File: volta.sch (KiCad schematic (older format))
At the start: 7 parts, among them J1 , J2 , T1 5:1 - 5A

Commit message: Trabajo
 Cambios para hacer commit:
	modificado:    volta-cache.lib
	modificado:    volta.kicad_pcb
	modificado:    volta.pro
	modificado:    volta.sch
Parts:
- removed J1, J2: (no value), Pin_Headers:Pin_Header_Straight_1x01_Pitch2.54mm, symbol Conn_01x01_Female
- removed T1: 5:1 - 5A, TerminalBlock:TerminalBlock_bornier-5_P5.08mm, symbol Transformer_1P_SS
- added C10, C6: 1uF, Capacitors_THT:CP_Radial_D5.0mm_P2.00mm, symbol EXI_Condensador_Polarizado
- added C11: 10uF, Capacitors_THT:CP_Radial_D5.0mm_P2.00mm, symbol EXI_Condensador_Polarizado
- added C3, C7: 0.33uF, Capacitors_THT:CP_Radial_D5.0mm_P2.00mm, symbol EXI_Condensador
- added C4, C8, C9: 0.1uF, Capacitors_THT:C_Disc_D5.0mm_W2.5mm_P2.50mm, symbol EXI_Condensador
- added C5: 22uF / 25V, Capacitors_THT:CP_Radial_D5.0mm_P2.00mm, symbol EXI_Condensador_Polarizado
- added D2, D3, D4, D5, D6: 1N4007, Diodes_THT:D_DO-41_SOD81_P10.16mm_Horizontal, symbol EXI_1N4007
- added J1: AC-vivo, EXI_Conectores:EXI_Pad_6x7mm_x1, symbol Conn_01x01
- added J10: +Vv, EXI_Conectores:EXI_Pad_6x7mm_x1, symbol Conn_01x01
- added J11: +5V, EXI_Conectores:EXI_Pad_6x7mm_x1, symbol Conn_01x01
- added J2: Trans-Vivo, EXI_Conectores:EXI_Pad_6x7mm_x1, symbol Conn_01x01
- added J3: Deriv, EXI_Conectores:EXI_Pad_6x7mm_x1, symbol Conn_01x01
- added J4: Trans-V24, EXI_Conectores:EXI_Pad_6x7mm_x1, symbol Conn_01x01
- added J5: Trans-N24, EXI_Conectores:EXI_Pad_6x7mm_x1, symbol Conn_01x01
- added J6: GND, EXI_Conectores:EXI_Pad_6x7mm_x1, symbol Conn_01x01
- added J7: V-, EXI_Conectores:EXI_Pad_6x7mm_x1, symbol Conn_01x01
- added J8: +12, EXI_Conectores:EXI_Pad_6x7mm_x1, symbol Conn_01x01
- added J9: -12, EXI_Conectores:EXI_Pad_6x7mm_x1, symbol Conn_01x01
- added MK1, MK2, MK3, MK4: Mounting_Hole, EXI_Montaje:Tuerca_9mm, symbol Mounting_Hole
- added POT1: 5k, TerminalBlock:TerminalBlock_bornier-3_P5.08mm, symbol EXI_Potenciómetro
- added POT2: 1k, TerminalBlock:TerminalBlock_bornier-3_P5.08mm, symbol EXI_Potenciómetro
- added R1: 120, Resistors_THT:R_Axial_DIN0309_L9.0mm_D3.2mm_P12.70mm_Horizontal, symbol EXI_Resistor
- added U1: L7812, EXI_Transistores:TO-220-3_Horizontal_Heatsink_10x15x21mm, symbol L7812
- added U2: L7912, EXI_Transistores:TO-220-3_Horizontal_Heatsink_10x15x21mm, symbol L7912
- added U3: L7805, EXI_Transistores:TO-220-3_Horizontal_Heatsink_10x15x21mm, symbol L7805
- added U4: LM338T, EXI_Transistores:TO-220-3_Horizontal_Heatsink_10x15x21mm, symbol LM338T
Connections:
- net labels added: +12, +12V, +5V, +Vv, -12, -12V, 120vAC / 60 hZ, 5:1 - 5A, Común, GNDPWR, Interruptor / Selector, LINE, NEUT, V+, V-, comun
- net labels removed: 120V / 60Hz
- wire segments 21 -> 93
- no-connect marks 0 -> 2
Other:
- moved on the sheet: C1, C2, D1, F1

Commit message: Cambios menores
 Cambios para hacer commit:
	agregado el modelo 3D del pin hecho en Wings3D al pcb
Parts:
- J1: footprint EXI_Conectores:EXI_Pad_6x7mm_x1 -> EXI_Conectores:terminal_faston_0.25

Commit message: Actualización
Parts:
- removed POT1: 5k, TerminalBlock:TerminalBlock_bornier-3_P5.08mm, symbol EXI_Potenciómetro
- removed POT2: 1k, TerminalBlock:TerminalBlock_bornier-3_P5.08mm, symbol EXI_Potenciómetro
- added J6: Pot_adj, EXI_Conectores:terminal_faston_0.25, symbol Conn_01x01
- added J7: Pot_gnd, EXI_Conectores:terminal_faston_0.25, symbol Conn_01x01
- added LED1: Activo, Pin_Headers:Pin_Header_Straight_1x02_Pitch2.54mm, symbol EXI_LED
- added R2: 470, Resistors_THT:R_Axial_DIN0309_L9.0mm_D3.2mm_P12.70mm_Horizontal, symbol EXI_Resistor
- added V1: EXI_Ventilador, symbol EXI_Ventilador
- J10: renamed from J8; footprint EXI_Conectores:EXI_Pad_6x7mm_x1 -> EXI_Conectores:terminal_faston_0.25
- J11: renamed from J9; footprint EXI_Conectores:EXI_Pad_6x7mm_x1 -> EXI_Conectores:terminal_faston_0.25
- J12: renamed from J10; footprint EXI_Conectores:EXI_Pad_6x7mm_x1 -> EXI_Conectores:terminal_faston_0.25
- J13: renamed from J11; footprint EXI_Conectores:EXI_Pad_6x7mm_x1 -> EXI_Conectores:terminal_faston_0.25
- J2: footprint EXI_Conectores:EXI_Pad_6x7mm_x1 -> EXI_Conectores:terminal_faston_0.25
- J3: renamed from J4; footprint EXI_Conectores:EXI_Pad_6x7mm_x1 -> EXI_Conectores:terminal_faston_0.25
- J4: renamed from J5; footprint EXI_Conectores:EXI_Pad_6x7mm_x1 -> EXI_Conectores:terminal_faston_0.25
- J5: renamed from J3; footprint EXI_Conectores:EXI_Pad_6x7mm_x1 -> EXI_Conectores:terminal_faston_0.25
- J8: renamed from J6; footprint EXI_Conectores:EXI_Pad_6x7mm_x1 -> EXI_Conectores:terminal_faston_0.25
- J9: renamed from J7; footprint EXI_Conectores:EXI_Pad_6x7mm_x1 -> EXI_Conectores:terminal_faston_0.25
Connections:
- net +5V: now also R2.1, V1.1 (+)
- net GND: now also V1.2 (-)
- net comun: now also J7.1 (Pin_1), LED1.2 (C)
- net sw: now reaches F1.1, J1.1 (Pin_1)
- net trans: now reaches F1.2, J2.1 (Pin_1)
- net v24: now reaches D1.2 (ac), J3.1 (Pin_1)
- net n24: now reaches D1.3 (ac), J4.1 (Pin_1)
- net adj: now reaches C11.1, D6.1 (A), R1.2, U4.1 (Adj)
- net adj: now also J6.1 (Pin_1)
- new net: LED1.1 (A), R2.2
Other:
- moved on the sheet: F1, J1, J2, J3, J4, J5

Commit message: Actualización mayor
cambio de pin blade 3.6
cambio de capacitores 3.3uF
cambio de pines para potenciometros
cambio de huella para fusible
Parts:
- removed C1, C2: 2200uF / 50V, Capacitors_THT:CP_Radial_D16.0mm_P7.50mm, symbol EXI_Condensador_Polarizado
- removed C10, C6: 1uF, Capacitors_THT:CP_Radial_D5.0mm_P2.00mm, symbol EXI_Condensador_Polarizado
- removed C11: 10uF, Capacitors_THT:CP_Radial_D5.0mm_P2.00mm, symbol EXI_Condensador_Polarizado
- removed C3, C7: 0.33uF, Capacitors_THT:CP_Radial_D5.0mm_P2.00mm, symbol EXI_Condensador
- removed C4, C8, C9: 0.1uF, Capacitors_THT:C_Disc_D5.0mm_W2.5mm_P2.50mm, symbol EXI_Condensador
- removed C5: 22uF / 25V, Capacitors_THT:CP_Radial_D5.0mm_P2.00mm, symbol EXI_Condensador_Polarizado
- removed D2, D3, D4, D5, D6: 1N4007, Diodes_THT:D_DO-41_SOD81_P10.16mm_Horizontal, symbol EXI_1N4007
- removed F1: Fusible, Fuse_Holders_and_Fuses:Fuseholder5x20_horiz_open_inline_Type-I, symbol EXI_Fusible
- removed LED1: Activo, Pin_Headers:Pin_Header_Straight_1x02_Pitch2.54mm, symbol EXI_LED
- removed R1: 120, Resistors_THT:R_Axial_DIN0309_L9.0mm_D3.2mm_P12.70mm_Horizontal, symbol EXI_Resistor
- removed R2: 470, Resistors_THT:R_Axial_DIN0309_L9.0mm_D3.2mm_P12.70mm_Horizontal, symbol EXI_Resistor
- added C1, C2: 2200uF / 50V, Capacitors_THT:CP_Radial_D16.0mm_P7.50mm, symbol CP
- added C10, C6: 1uF, Capacitors_THT:CP_Radial_D5.0mm_P2.00mm, symbol CP
- added C11: 10uF, Capacitors_THT:CP_Radial_D5.0mm_P2.00mm, symbol CP
- added C3, C7: 0.33uF, Capacitors_THT:C_Disc_D9.0mm_W2.5mm_P5.00mm, symbol C
- added C4, C8, C9: 0.1uF, Capacitors_THT:C_Disc_D5.0mm_W2.5mm_P2.50mm, symbol C
- added C5: 22uF, Capacitors_THT:CP_Radial_D5.0mm_P2.00mm, symbol CP
- added D2, D3, D4, D5, D6: 1N4007, Diodes_THT:D_DO-41_SOD81_P7.62mm_Horizontal, symbol 1N4007
- added D7: Activo, Pin_Headers:Pin_Header_Straight_1x02_Pitch2.54mm, symbol LED
- added F1: Fusible, Fuse_Holders_and_Fuses:Fuseholder5x20_horiz_open_universal_Type-III, symbol Fuse
- added R1: 120, Resistors_THT:R_Axial_DIN0309_L9.0mm_D3.2mm_P12.70mm_Horizontal, symbol R
- added R2: 470, Resistors_THT:R_Axial_DIN0309_L9.0mm_D3.2mm_P12.70mm_Horizontal, symbol R
- J1, J10, J11, J12, J13, J2, J3, J4, J5, J8, J9: footprint EXI_Conectores:terminal_faston_0.25 -> EXI_Conectores:blade_vertical_6.3mm_P5.08mm
- J6, J7: footprint EXI_Conectores:terminal_faston_0.25 -> Pin_Headers:Pin_Header_Straight_1x01_Pitch2.54mm
- V1: footprint (none) -> Pin_Headers:Pin_Header_Straight_1x02_Pitch2.54mm
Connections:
- net +12: now also C4.1, D2.1 (K)
- net +5V: now also C8.1, D4.1 (K), R2.1
- net +Vv: now also C10.1, D5.2 (A), D6.1 (K), R1.1
- net -12: now also C6.2, D3.2 (A)
- net GND: now also C1.2, C2.1, C3.2, C4.2, C5.1, C6.1, D2.2 (A), D3.1 (K); no longer V1.2 (-)
- net V-: now also C2.2; no longer U2.2 (VI)
- net adj: now also C11.1, D6.2 (A), R1.2
- net comun: no longer U3.2 (GND)
- net sw: now also F1.2
- net trans: now also F1.1
- net V+ renamed +VDC
- net +VDC: now also C1.1, C3.1, C7.1, C9.1, D5.1 (K)
- new net: D7.2 (A), R2.2
- new net -VDC: C5.2, U2.2 (VI)
- new net GNDREF: C10.2, C11.2, C7.2, C8.2, C9.2, D4.2 (A), D7.1 (K), U3.2 (GND), V1.2 (-)
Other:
- note added: "Extras"
- note added: "Reducción, Rectificación y Filtrado"
- note added: "Referencias"
- note added: "Regulación Variable"
- note added: "Regulación fija +5V"
- note added: "Regulación simétrica +/- 12V"
- note added: "Selector de salidas"
- note removed: "Alimentaciones"
- moved on the sheet: D1, J1, J10, J11, J12, J13, J2, J3, J4, J5, J6, J7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

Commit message: nuevo cajetin de udeg
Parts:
- removed D7: Activo, Pin_Headers:Pin_Header_Straight_1x02_Pitch2.54mm, symbol LED
- removed J6: Pot_adj, Pin_Headers:Pin_Header_Straight_1x01_Pitch2.54mm, symbol Conn_01x01
- removed J7: Pot_gnd, Pin_Headers:Pin_Header_Straight_1x01_Pitch2.54mm, symbol Conn_01x01
- removed V1: EXI_Ventilador, Pin_Headers:Pin_Header_Straight_1x02_Pitch2.54mm, symbol EXI_Ventilador
- added J101: Perifericos, Pin_Headers:Pin_Header_Straight_1x04_Pitch2.54mm, symbol Conn_01x04
- C10: footprint Capacitors_THT:CP_Radial_D5.0mm_P2.00mm -> Capacitors_THT:CP_Radial_D5.0mm_P2.50mm
- C3, C4, C7, C8, C9: symbol C -> C-RESCUE-volta
- R1, R2: symbol R -> R-RESCUE-volta
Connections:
- net +5V: now also J101.4 (Pin_4)
- net GNDREF: now also J101.1 (Pin_1)
- net adj: now also J101.2 (Pin_2)
- net LED: now reaches R2.2
- net LED: now also J101.3 (Pin_3)

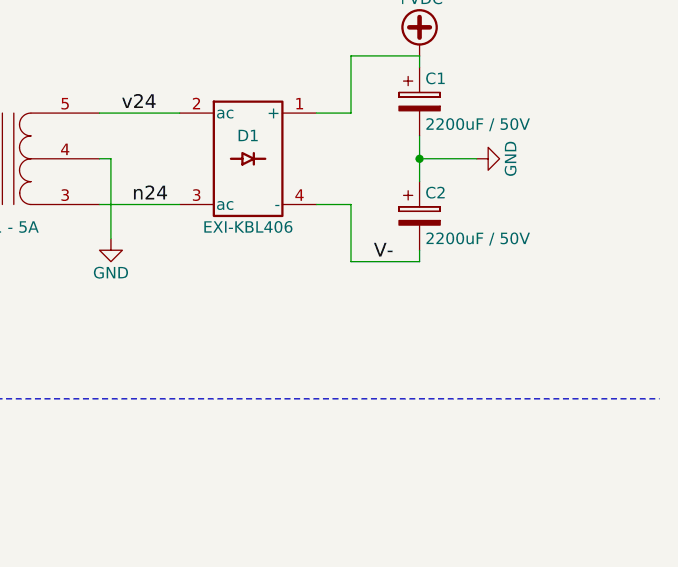
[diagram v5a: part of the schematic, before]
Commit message: avanzada en la PCB con plano de tierra
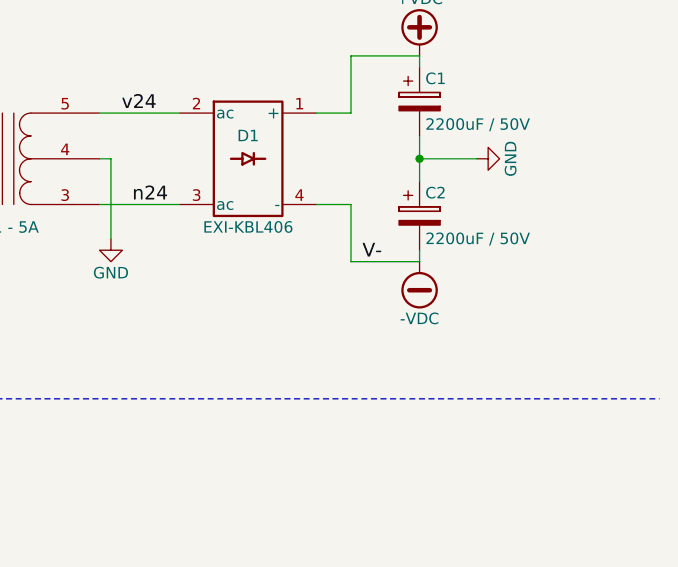
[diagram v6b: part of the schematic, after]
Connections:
- net V- is gone; now on net -VDC: C2.2, D1.4 (-), J9.1 (Pin_1)
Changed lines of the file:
@@
 LIBS:EXI_Transistores
 LIBS:EXI_Varios
-LIBS:Amplifier_Audio
-LIBS:Amplifier_Buffer
-LIBS:Amplifier_Current
-LIBS:Amplifier_Difference
-LIBS:Amplifier_Instrumentation
-LIBS:Amplifier_Operational
-LIBS:Amplifier_Video
-LIBS:Analog
-LIBS:Analog_ADC
-LIBS:Analog_DAC
-LIBS:Analog_Switch
-LIBS:Audio
-LIBS:Battery_Management
-LIBS:Comparator
-LIBS:Connector_Generic
-LIBS:Connector_Generic_Shielded
-LIBS:Connector_Specialized
-LIBS:Converter_ACDC
-LIBS:Converter_DCDC
-LIBS:CPLD_Altera
-LIBS:CPLD_Xilinx
-LIBS:CPU
-LIBS:CPU_NXP_6800
-LIBS:CPU_NXP_68000
-LIBS:CPU_PowerPC
-LIBS:Device
-LIBS:Diode
-LIBS:Diode_Bridge
-LIBS:Diode_Laser
-LIBS:Display_Character
-LIBS:Display_Graphic
-LIBS:Driver_Display
-LIBS:Driver_FET
-LIBS:Driver_LED
-LIBS:Driver_Motor
-LIBS:Driver_Relay
-LIBS:DSP_Freescale
-LIBS:DSP_Microchip_DSPIC33
-LIBS:DSP_Motorola
-LIBS:DSP_Texas
-LIBS:Filter
-LIBS:FPGA_Actel
-LIBS:FPGA_Xilinx
-LIBS:FPGA_Xilinx_Artix7
-LIBS:FPGA_Xilinx_Kintex7
-LIBS:FPGA_Xilinx_Spartan6
-LIBS:FPGA_Xilinx_Virtex5
-LIBS:FPGA_Xilinx_Virtex6
-LIBS:FPGA_Xilinx_Virtex7
-LIBS:GPU
-LIBS:Graphic
-LIBS:Interface
-LIBS:Interface_CAN_LIN
-LIBS:Interface_CurrentLoop
-LIBS:Interface_Ethernet
-LIBS:Interface_Expansion
-LIBS:Interface_HID
-LIBS:Interface_LineDriver
-LIBS:Interface_Optical
-LIBS:Interface_Telecom
-LIBS:Interface_UART
-LIBS:Interface_USB
-LIBS:Isolator
-LIBS:Isolator_Analog
-LIBS:Jumper
-LIBS:LED
-LIBS:Logic_74xgxx
-LIBS:Logic_74xx
-LIBS:Logic_CMOS_4000
-LIBS:Logic_CMOS_IEEE
-LIBS:Logic_LevelTranslator
-LIBS:Logic_Programmable
-LIBS:Logic_TTL_IEEE
-LIBS:MCU_AnalogDevices
-LIBS:MCU_Atmel_8051
-LIBS:MCU_Atmel_ATMEGA
-LIBS:MCU_Atmel_ATTINY
-LIBS:MCU_Atmel_AVR
-LIBS:MCU_Cypress
-LIBS:MCU_Infineon
-LIBS:MCU_Intel
-LIBS:MCU_Microchip_PIC10
-LIBS:MCU_Microchip_PIC12
-LIBS:MCU_Microchip_PIC16
-LIBS:MCU_Microchip_PIC18
-LIBS:MCU_Microchip_PIC24
-LIBS:MCU_Microchip_PIC32
-LIBS:MCU_Microchip_SAME
-LIBS:MCU_Microchip_SAML
-LIBS:MCU_Module
-LIBS:MCU_NXP_ColdFire
-LIBS:MCU_NXP_HC11
-LIBS:MCU_NXP_HC12
-LIBS:MCU_NXP_HCS12
-LIBS:MCU_NXP_Kinetis
-LIBS:MCU_NXP_LPC
-LIBS:MCU_NXP_MAC7100
-LIBS:MCU_NXP_MCore
-LIBS:MCU_NXP_S08
-LIBS:MCU_Parallax
-LIBS:MCU_SiFive
-LIBS:MCU_SiliconLabs
-LIBS:MCU_ST_STM8
-LIBS:MCU_ST_STM32
-LIBS:MCU_Texas
-LIBS:MCU_Texas_MSP430
-LIBS:Mechanical
-LIBS:Memory_Controller
-LIBS:Memory_EEPROM
-LIBS:Memory_EPROM
-LIBS:Memory_Flash
-LIBS:Memory_NVRAM
-LIBS:Memory_RAM
-LIBS:Memory_ROM
-LIBS:Memory_UniqueID
-LIBS:Motor
-LIBS:Oscillator
-LIBS:Potentiometer_Digital
 LIBS:power
 LIBS:Power_Management
-LIBS:Power_Protection
-LIBS:Power_Supervisor
 LIBS:pspice
-LIBS:Reference_Current
-LIBS:Reference_Voltage
-LIBS:Regulator_Controller
-LIBS:Regulator_Current
-LIBS:Regulator_Linear
-LIBS:Regulator_SwitchedCapacitor
-LIBS:Regulator_Switching
-LIBS:Relay
-LIBS:Relay_SolidState
-LIBS:RF
-LIBS:RF_AM_FM
-LIBS:RF_Bluetooth
-LIBS:RF_GPS
-LIBS:RF_Mixer
-LIBS:RF_Module
-LIBS:RF_RFID
-LIBS:RF_WiFi
-LIBS:RF_ZigBee
-LIBS:Sensor
-LIBS:Sensor_Audio
-LIBS:Sensor_Current
-LIBS:Sensor_Gas
-LIBS:Sensor_Humidity
-LIBS:Sensor_Magnetic
-LIBS:Sensor_Motion
-LIBS:Sensor_Optical
-LIBS:Sensor_Pressure
-LIBS:Sensor_Proximity
-LIBS:Sensor_Temperature
-LIBS:Sensor_Touch
-LIBS:Sensor_Voltage
-LIBS:Switch
-LIBS:Timer
-LIBS:Timer_PLL
-LIBS:Timer_RTC
-LIBS:Transformer
-LIBS:Transistor_Array
-LIBS:Transistor_BJT
-LIBS:Transistor_FET
-LIBS:Transistor_IGBT
-LIBS:Triac_Thyristor
-LIBS:Valve
-LIBS:Video
 LIBS:volta-cache
 EELAYER 25 0
@@
 $EndComp
 $Comp
-L EXI_KDC3 #IN101
+L EXI_KDC3 #IN1
 U 1 1 5ACCC4F9
 P 3550 2150
-F 0 "#IN101" H 3750 2300 40  0001 R CNN
+F 0 "#IN1" H 3750 2300 40  0001 R CNN
 F 1 "KDC3" H 3550 2050 40  0000 C CNN
 F 2 "" H 3650 2150 60  0000 C CNN
@@
 	0    -1   -1   0
 $EndComp
-Text Label 6650 2800 0    60   ~ 0
-V-
 $Comp
 L L7812 U1
@@
 NoConn ~ 5800 8050
 $Comp
-L Conmutador_3p2t #IN102
+L Conmutador_3p2t #IN2
 U 1 1 5ACFA9C1
 P 6100 7650
-F 0 "#IN102" H 6100 8150 50  0001 C CNN
+F 0 "#IN2" H 6100 8150 50  0001 C CNN
 F 1 "Interruptor / Selector" H 6100 8150 50  0000 C CNN
 F 2 "TerminalBlock_4UCON:TerminalBlock_4UCON_19963_09x3.5mm_Straight" H 6100 7350 60  0001 C CNN
@@
 $EndComp
 $Comp
-L Conn_01x03_Female #J101
+L Conn_01x03_Female #J1
 U 1 1 5ACFD97A
 P 2700 2200
-F 0 "#J101" H 2700 2400 50  0001 C CNN
+F 0 "#J1" H 2700 2400 50  0001 C CNN
 F 1 "120vAC / 60 hZ" H 2700 1900 50  0000 C CNN
 F 2 "" H 2700 2200 50  0001 C CNN
@@
 trans
 $Comp
-L Transformer_1P_SS #T101
+L Transformer_1P_SS #T1
 U 1 1 5ACCC90F
 P 5050 2350
-F 0 "#T101" H 5050 2600 50  0001 C CNN
+F 0 "#T1" H 5050 2600 50  0001 C CNN
 F 1 "5:1 - 5A" H 5050 2050 50  0000 C CNN
 F 2 "" H 5050 2350 50  0001 C CNN
@@
 v24
 $Comp
-L Conn_01x01_Female #J106
+L Conn_01x01_Female #J6
 U 1 1 5ACFB14C
 P 7050 8550
-F 0 "#J106" H 7050 8650 50  0001 C CNN
+F 0 "#J6" H 7050 8650 50  0001 C CNN
 F 1 "+5V" H 7150 8550 50  0000 C CNN
 F 2 "" H 7050 8550 50  0001 C CNN
@@
 $EndComp
 $Comp
-L Conn_01x01_Female #J105
+L Conn_01x01_Female #J5
 U 1 1 5ACFB0AE
 P 7050 8250
-F 0 "#J105" H 7050 8350 50  0001 C CNN
+F 0 "#J5" H 7050 8350 50  0001 C CNN
 F 1 "+Vv" H 7150 8250 50  0000 C CNN
 F 2 "" H 7050 8250 50  0001 C CNN
@@
 $EndComp
 $Comp
-L Conn_01x01_Female #J104
+L Conn_01x01_Female #J4
 U 1 1 5ACFAFA0
 P 7050 7950
-F 0 "#J104" H 7050 8050 50  0001 C CNN
+F 0 "#J4" H 7050 8050 50  0001 C CNN
 F 1 "-12V" H 7200 7950 50  0000 C CNN
 F 2 "" H 7050 7950 50  0001 C CNN
@@
 $EndComp
 $Comp
-L Conn_01x01_Female #J103
+L Conn_01x01_Female #J3
 U 1 1 5ACFAF0C
 P 7050 7650
-F 0 "#J103" H 7050 7750 50  0001 C CNN
+F 0 "#J3" H 7050 7750 50  0001 C CNN
 F 1 "+12V" H 7200 7650 50  0000 C CNN
 F 2 "" H 7050 7650 50  0001 C CNN
@@
 $EndComp
 $Comp
-L Conn_01x01_Female #J102
+L Conn_01x01_Female #J2
 U 1 1 5ACFACC5
 P 7050 7350
-F 0 "#J102" H 7050 7450 50  0001 C CNN
+F 0 "#J2" H 7050 7450 50  0001 C CNN
 F 1 "Común" H 7250 7350 50  0000 C CNN
 F 2 "" H 7050 7350 50  0001 C CNN
@@
 +5V
 $Comp
-L EXI_Ventilador #V101
+L EXI_Ventilador #V1
 U 1 1 5AD63847
 P 2650 9750
-F 0 "#V101" H 2750 9550 50  0001 C CNN
+F 0 "#V1" H 2750 9550 50  0001 C CNN
 F 1 "EXI_Ventilador" H 2750 9950 50  0000 C CNN
 F 2 "" H 2750 9750 118 0001 C CNN
@@
 $EndComp
 $Comp
-L POT #RV101
+L POT #RV1
 U 1 1 5ADFA282
 P 1700 7900
-F 0 "#RV101" V 1525 7900 50  0001 C CNN
+F 0 "#RV1" V 1525 7900 50  0001 C CNN
 F 1 "5k" V 1600 7900 50  0000 C CNN
 F 2 "" H 1700 7900 50  0001 C CNN
@@
 $EndComp
 $Comp
-L POT #RV102
+L POT #RV2
 U 1 1 5ADFA3A1
 P 1700 8300
-F 0 "#RV102" V 1525 8300 50  0001 C CNN
+F 0 "#RV2" V 1525 8300 50  0001 C CNN
 F 1 "1k" V 1600 8300 50  0000 C CNN
 F 2 "" H 1700 8300 50  0001 C CNN
@@
 $EndComp
 $Comp
-L LED #D101
+L LED #D1
 U 1 1 5ADFC202
 P 1450 9900
-F 0 "#D101" H 1450 10000 50  0001 C CNN
+F 0 "#D1" H 1450 10000 50  0001 C CNN
 F 1 "Activo" H 1450 9800 50  0000 C CNN
 F 2 "" H 1450 9900 50  0001 C CNN
@@
 Wire Wire Line
 	3550 7700 3850 7700
+$Comp
+L -VDC #PWR034
+U 1 1 5B2C4332
+P 6850 2800
+F 0 "#PWR034" H 6850 2700 50  0001 C CNN
+F 1 "-VDC" H 6850 3050 50  0000 C CNN
+F 2 "" H 6850 2800 50  0001 C CNN
+F 3 "" H 6850 2800 50  0001 C CNN
+	1    6850 2800
+	-1   0    0    1
+$EndComp
+Text Label 6600 2800 0    60   ~ 0
+V-
 $EndSCHEMATC
